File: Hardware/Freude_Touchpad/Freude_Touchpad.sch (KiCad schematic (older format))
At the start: 10 parts, among them J1 Conn_01x06_Female, U1 IQS572, X1 Custom_Touchpad

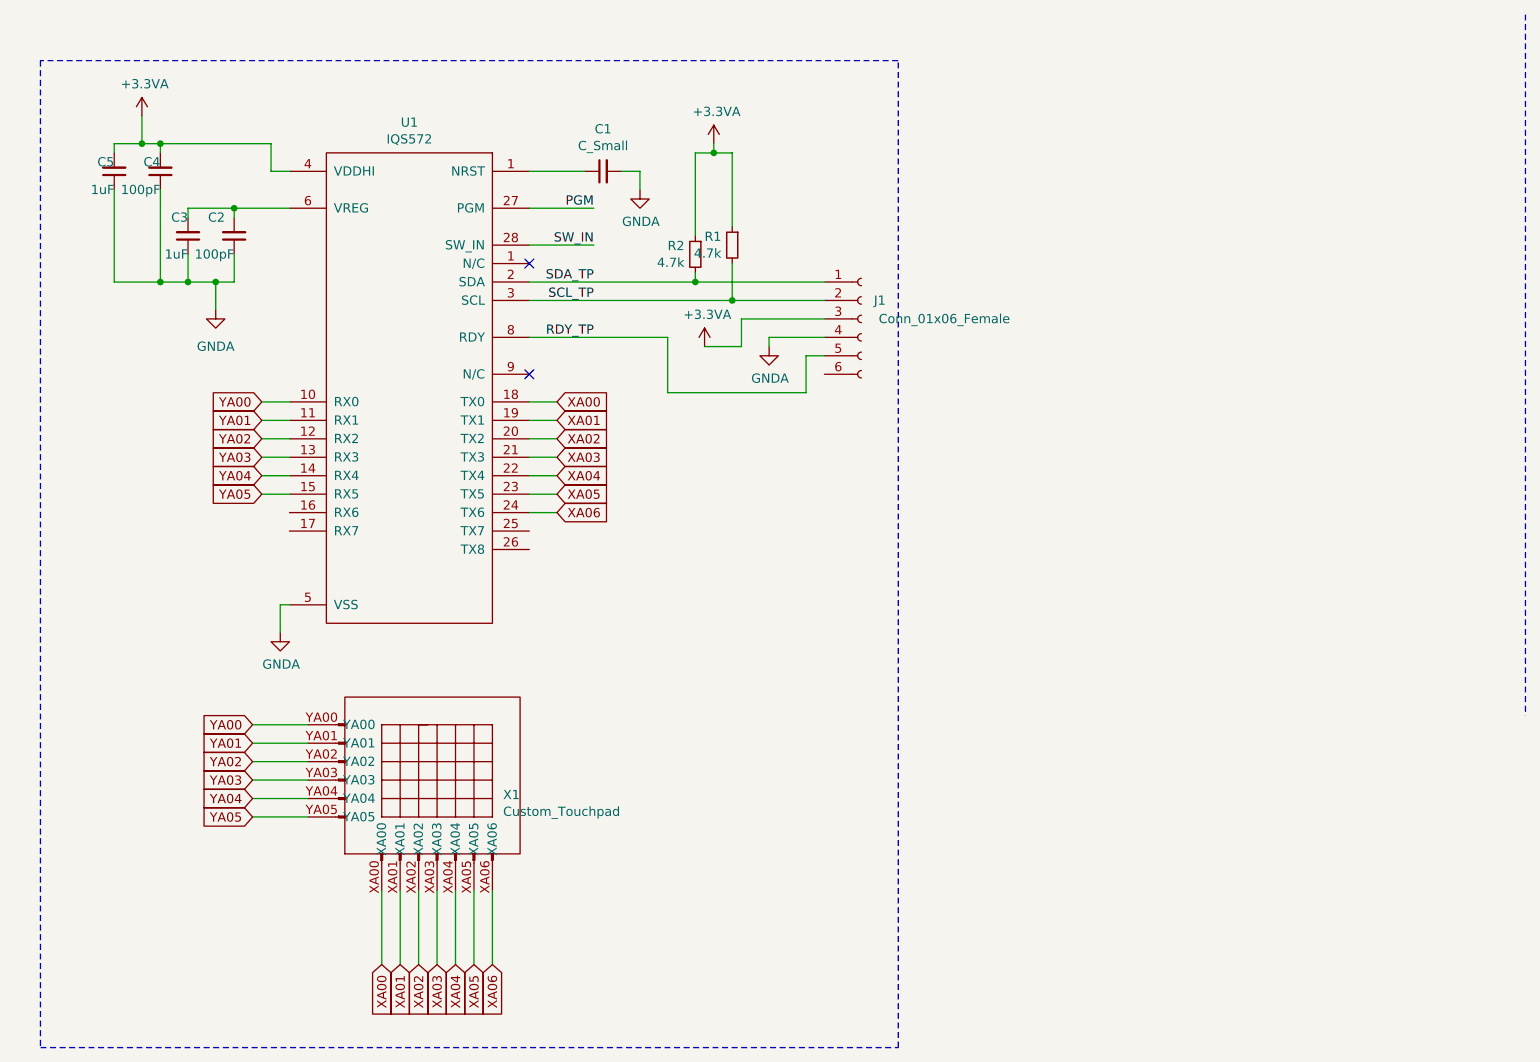
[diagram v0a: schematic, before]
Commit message: added ground pour and ground ring
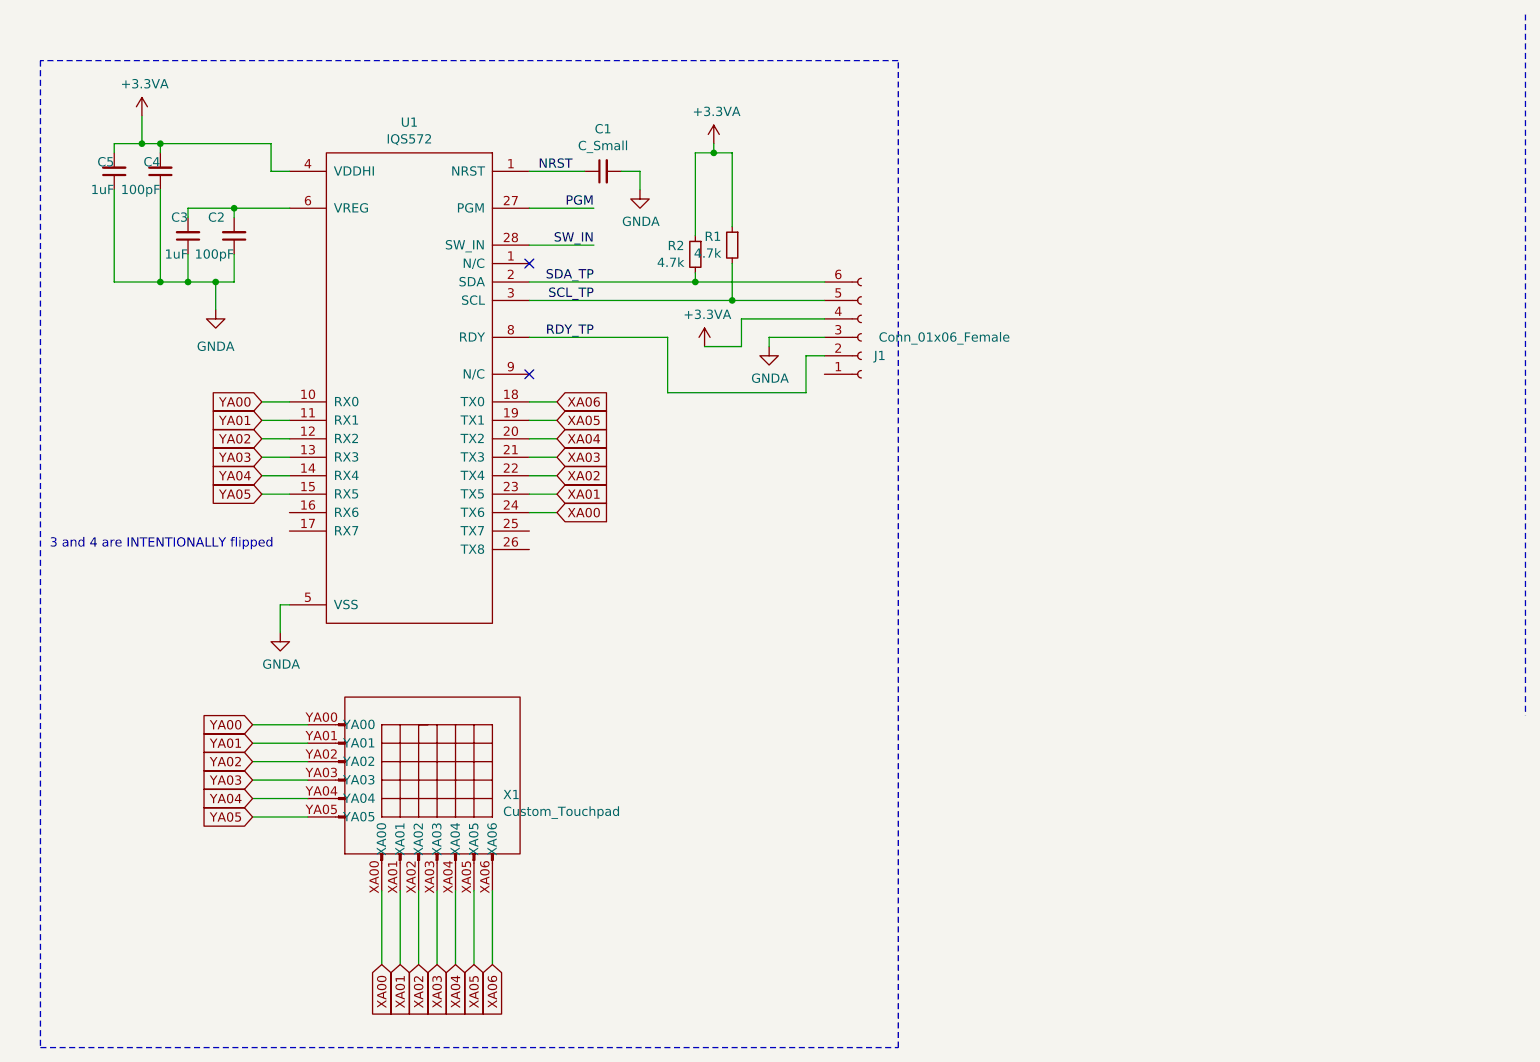
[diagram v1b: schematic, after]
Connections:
- net +3.3VA: now also J1.4 (Pin_4); no longer J1.3 (Pin_3)
- net GNDA: now also J1.3 (Pin_3); no longer J1.4 (Pin_4)
- net RDY_TP: now also J1.2 (Pin_2); no longer J1.5 (Pin_5)
- net SCL_TP: now also J1.5 (Pin_5); no longer J1.2 (Pin_2)
- net SDA_TP: now also J1.6 (Pin_6); no longer J1.1 (Pin_1)
- net XA00: now also U1.24 (TX6); no longer U1.18 (TX0)
- net XA01: now also U1.23 (TX5); no longer U1.19 (TX1)
- net XA02: now also U1.22 (TX4); no longer U1.20 (TX2)
- net XA04: now also U1.20 (TX2); no longer U1.22 (TX4)
- net XA05: now also U1.19 (TX1); no longer U1.23 (TX5)
- net XA06: now also U1.18 (TX0); no longer U1.24 (TX6)
- net NRST: now reaches U1.1 (NRST)
- net NRST: now also C1.1
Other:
- note added: "3 and 4 are INTENTIONALLY flipped"
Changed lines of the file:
@@
 Comment4 ""
 $EndDescr
+Text GLabel 5850 3300 2    50   Input ~ 0
+XA00
+Text GLabel 5850 3200 2    50   Input ~ 0
+XA01
+Text GLabel 5850 3100 2    50   Input ~ 0
+XA02
+Text GLabel 5850 2900 2    50   Input ~ 0
+XA04
 Text GLabel 5850 2700 2    50   Input ~ 0
-XA00
-Text GLabel 5850 2800 2    50   Input ~ 0
-XA01
-Text GLabel 5850 2900 2    50   Input ~ 0
-XA02
-Text GLabel 5850 3100 2    50   Input ~ 0
-XA04
-Text GLabel 5850 3300 2    50   Input ~ 0
 XA06
 Text GLabel 5850 3000 2    50   Input ~ 0
 XA03
-Text GLabel 5850 3200 2    50   Input ~ 0
+Text GLabel 5850 2800 2    50   Input ~ 0
 XA05
 Wire Wire Line
@@
 	6600 1350 6600 1800
 Wire Wire Line
-	6000 1450 5700 1450
-Wire Wire Line
 	6300 1550 6300 1450
 Wire Wire Line
@@
 Wire Wire Line
 	4200 4950 4500 4950
-Text GLabel 4900 5750 3    50   Input ~ 0
-XA00
-Text GLabel 5000 5750 3    50   Input ~ 0
-XA01
-Text GLabel 5100 5750 3    50   Input ~ 0
-XA02
-Text GLabel 5300 5750 3    50   Input ~ 0
-XA04
-Text GLabel 5500 5750 3    50   Input ~ 0
-XA06
-Text GLabel 5200 5750 3    50   Input ~ 0
-XA03
-Text GLabel 5400 5750 3    50   Input ~ 0
-XA05
-Wire Wire Line
-	4900 5750 4900 5350
-Wire Wire Line
-	5000 5350 5000 5750
-Wire Wire Line
-	5100 5750 5100 5350
-Wire Wire Line
-	5200 5350 5200 5750
-Wire Wire Line
-	5300 5750 5300 5350
-Wire Wire Line
-	5400 5350 5400 5750
-Wire Wire Line
-	5500 5750 5500 5350
 Wire Wire Line
 	6800 1350 6800 1750
@@
 L Connector:Conn_01x06_Female J1
 U 1 1 5F1F693D
-P 7500 2250
-F 0 "J1" H 7600 2350 50  0000 C CNN
-F 1 "Conn_01x06_Female" H 7950 2250 50  0000 C CNN
-F 2 ".pretty:503480-0600" H 7500 2250 50  0001 C CNN
-F 3 "~" H 7500 2250 50  0001 C CNN
-	1    7500 2250
-	1    0    0    -1
+P 7500 2350
+F 0 "J1" H 7600 2450 50  0000 C CNN
+F 1 "Conn_01x06_Female" H 7950 2350 50  0000 C CNN
+F 2 ".pretty:503480-0600" H 7500 2350 50  0001 C CNN
+F 3 "~" H 7500 2350 50  0001 C CNN
+	1    7500 2350
+	1    0    0    1
 $EndComp
 Wire Wire Line
@@
 Wire Wire Line
 	7300 2450 7200 2450
+Wire Wire Line
+	5500 5750 5500 5350
+Wire Wire Line
+	5400 5350 5400 5750
+Wire Wire Line
+	5300 5750 5300 5350
+Wire Wire Line
+	5200 5350 5200 5750
+Wire Wire Line
+	5100 5750 5100 5350
+Wire Wire Line
+	5000 5350 5000 5750
+Wire Wire Line
+	4900 5750 4900 5350
+Text GLabel 5400 5750 3    50   Input ~ 0
+XA05
+Text GLabel 5200 5750 3    50   Input ~ 0
+XA03
+Text GLabel 5300 5750 3    50   Input ~ 0
+XA04
+Text GLabel 5100 5750 3    50   Input ~ 0
+XA02
+Text GLabel 5000 5750 3    50   Input ~ 0
+XA01
+Text GLabel 4900 5750 3    50   Input ~ 0
+XA00
+Text GLabel 5500 5750 3    50   Input ~ 0
+XA06
+Text Notes 3100 3500 0    50   ~ 0
+3 and 4 are INTENTIONALLY flipped
+Text Label 5750 1450 0    50   ~ 0
+NRST
+Wire Wire Line
+	5700 1450 6000 1450
 $EndSCHEMATC

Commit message: resolves 10, resolves 9, resolves 6, resolves 5, add ground ring around touch sensor, add ground ring on top, separate RX from TX and include ground plane between
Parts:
- added TP01, TP02: TestPoint, Measurement_Points:Measurement_Point_Square-SMD-Pad_Small, symbol Connector:TestPoint
- C1: value C_Small -> 100nf
- X1: footprint Custom_Touchpad:Touchpad -> (none); symbol Custom_Touchpad:Custom_Touchpad -> Custom_Touchpad:Custom_Touchpad5x5
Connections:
- net labels removed: XA06
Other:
- note added: "YA05 and YA04 are intentionally\nswitched. The IQS572 can \ncompensate for this. See page\n20 of datasheet."
- note removed: "3 and 4 are INTENTIONALLY flipped"
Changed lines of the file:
@@
 Text GLabel 5850 2900 2    50   Input ~ 0
 XA04
-Text GLabel 5850 2700 2    50   Input ~ 0
-XA06
 Text GLabel 5850 3000 2    50   Input ~ 0
 XA03
@@
 Text GLabel 4250 3000 0    50   Input ~ 0
 YA03
+Text GLabel 4250 3200 0    50   Input ~ 0
+YA04
 Text GLabel 4250 3100 0    50   Input ~ 0
-YA04
-Text GLabel 4250 3200 0    50   Input ~ 0
 YA05
 Wire Wire Line
@@
 	4250 3000 4400 3000
 Wire Wire Line
-	4400 3100 4250 3100
-Wire Wire Line
-	4250 3200 4400 3200
-Wire Wire Line
-	5850 2700 5700 2700
+	4400 3200 4250 3200
+Wire Wire Line
+	4250 3100 4400 3100
 Wire Wire Line
 	5700 2800 5850 2800
@@
 P 6100 1450
 F 0 "C1" V 5871 1450 50  0000 C CNN
-F 1 "C_Small" V 5962 1450 50  0000 C CNN
+F 1 "100nf" V 5962 1450 50  0000 C CNN
 F 2 "Resistors_SMD:R_0402" H 6100 1450 50  0001 C CNN
 F 3 "~" H 6100 1450 50  0001 C CNN
@@
 	3700 2050 3850 2050
 Wire Wire Line
-	3700 1300 4300 1300
-Wire Wire Line
-	3450 2050 3700 2050
+	3700 1300 3950 1300
+Wire Wire Line
+	3450 2050 3500 2050
 Connection ~ 3600 1300
 Wire Wire Line
@@
 	7000 2350 7000 2400
 $Comp
-L Custom_Touchpad:Custom_Touchpad X1
+L Custom_Touchpad:Custom_Touchpad5x5 X1
 U 1 1 5F1BAD65
 P 4700 4950
 F 0 "X1" H 5558 5070 50  0000 L CNN
 F 1 "Custom_Touchpad" H 5558 4979 50  0000 L CNN
-F 2 "Custom_Touchpad:Touchpad" H 4700 4950 50  0001 C CNN
+F 2 "" H 4700 4950 50  0001 C CNN
 F 3 "" H 4700 4950 50  0001 C CNN
 	1    4700 4950
@@
 Wire Wire Line
 	7300 2450 7200 2450
-Wire Wire Line
-	5500 5750 5500 5350
 Wire Wire Line
 	5400 5350 5400 5750
@@
 Text GLabel 4900 5750 3    50   Input ~ 0
 XA00
-Text GLabel 5500 5750 3    50   Input ~ 0
-XA06
-Text Notes 3100 3500 0    50   ~ 0
-3 and 4 are INTENTIONALLY flipped
 Text Label 5750 1450 0    50   ~ 0
 NRST
 Wire Wire Line
 	5700 1450 6000 1450
+Text Notes 3100 3650 0    50   ~ 0
+YA05 and YA04 are intentionally\nswitched. The IQS572 can \ncompensate for this. See page\n20 of datasheet.
+$Comp
+L Connector:TestPoint TP01
+U 1 1 5FBD9D21
+P 3950 1300
+F 0 "TP01" H 4008 1418 50  0000 L CNN
+F 1 "TestPoint" H 4008 1327 50  0000 L CNN
+F 2 "Measurement_Points:Measurement_Point_Square-SMD-Pad_Small" H 4150 1300 50  0001 C CNN
+F 3 "~" H 4150 1300 50  0001 C CNN
+	1    3950 1300
+	1    0    0    -1
+$EndComp
+Connection ~ 3950 1300
+Wire Wire Line
+	3950 1300 4300 1300
+$Comp
+L Connector:TestPoint TP02
+U 1 1 5FBE3310
+P 3500 2050
+F 0 "TP02" H 3450 2200 50  0000 R CNN
+F 1 "TestPoint" H 3550 2300 50  0000 R CNN
+F 2 "Measurement_Points:Measurement_Point_Square-SMD-Pad_Small" H 3700 2050 50  0001 C CNN
+F 3 "~" H 3700 2050 50  0001 C CNN
+	1    3500 2050
+	-1   0    0    1
+$EndComp
+Connection ~ 3500 2050
+Wire Wire Line
+	3500 2050 3700 2050
 $EndSCHEMATC
